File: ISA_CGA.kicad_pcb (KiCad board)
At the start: 4 copper layers, 337.6 x 105.7 mm, 168 parts, among them J1 VIDEO JACK, J2 RGBI Output, P1 1X4 BERG, P2 1X6 BERG, P5 Bus_ISA_8bit, Q1 2N3904, U1 74S112, U10 74153, U101 74S174, U11 74LS74, U12 74LS393, U13 74LS08, U14 74S32, U15 74LS00, U16 74LS04, U17 74LS138, U18 74LS138, U19 74LS138, U2 74LS74, U20 74LS04, U21 74LS174, U22 74LS51, U23 74LS32, U24 74LS244, U25 74LS00, U26 74S04, U27 74LS51, U28 74LS10, U29 74S04, U3 74S86, U30 74LS32, U31 74S08, U32 74LS166, U33 27C256, U34 74LS273, U35 74LS273, U36 74LS244, U37 74LS374, U38 MC6845, U39 74LS174, U4 74S174, U40 74LS174, U41 74LS08, U42 74LS86, U43 74S74, U44 74S74, U45 74LS151, U46 74LS00, U47 74LS51, U48 74LS51, U49 74LS02, U5 74S174, U50 2118, U51 2118, U52 2118, U53 2118, U54 2118, U55 2118, U56 2118, U57 2118, U58 74LS374, U59 74LS374, U6 74LS04, U60 74LS374, U61 74LS374, U62 74LS125, U63 74LS175, U64 74LS164, U65 74LS02, U66 74LS245, U67 74LS244, U68 74LS86, U7 74LS166, U8 74LS166, U9 74153

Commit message: Added copper fill zones
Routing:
- added copper zone on B.Cu, net GND
- added copper zone on F.Cu, net GND
- added copper zone on In1.Cu, net GND
- added copper zone on In2.Cu, net VCC
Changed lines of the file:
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@@
     (connect_pads (clearance 0.508))
     (min_thickness 0.254)
-    (fill yes (arc_segments 32) (thermal_gap 0.508) (thermal_bridge_width 0.508))
+    (fill (arc_segments 32) (thermal_gap 0.508) (thermal_bridge_width 0.508))
     (polygon
       (pts
@@
     (connect_pads (clearance 0.508))
     (min_thickness 0.254)
-    (fill yes (arc_segments 32) (thermal_gap 0.508) (thermal_bridge_width 0.508))
+    (fill (arc_segments 32) (thermal_gap 0.508) (thermal_bridge_width 0.508))
     (polygon
       (pts
@@
       )
     )
+  )
+  (zone (net 2) (net_name GND) (layer B.Cu) (hatch edge 0.508)
+    (connect_pads (clearance 0.508))
+    (min_thickness 0.254)
+    (fill (arc_segments 32) (thermal_gap 0.508) (thermal_bridge_width 0.508))
+    (polygon
+      (pts
+        (xy 376.301 172.212) (xy 260.35 172.212) (xy 260.35 187.706) (xy 30.48 187.706) (xy 30.48 65.659)
+        (xy 376.174 65.659) (xy 376.301 65.532)
+      )
+    )
+  )
+  (zone (net 2) (net_name GND) (layer In1.Cu) (hatch edge 0.508)
+    (connect_pads (clearance 0.508))
+    (min_thickness 0.254)
+    (fill (arc_segments 32) (thermal_gap 0.508) (thermal_bridge_width 0.508))
+    (polygon
+      (pts
+        (xy 376.301 172.198383) (xy 260.35 172.198383) (xy 260.35 187.692383) (xy 30.48 187.692383) (xy 30.48 65.645383)
+        (xy 376.174 65.645383) (xy 376.301 65.518383)
+      )
+    )
+  )
+  (zone (net 2) (net_name GND) (layer F.Cu) (hatch edge 0.508)
+    (connect_pads (clearance 0.508))
+    (min_thickness 0.254)
+    (fill (arc_segments 32) (thermal_gap 0.508) (thermal_bridge_width 0.508))
+    (polygon
+      (pts
+        (xy 376.301 172.198383) (xy 260.35 172.198383) (xy 260.35 187.692383) (xy 30.48 187.692383) (xy 30.48 65.645383)
+        (xy 376.174 65.645383) (xy 376.301 65.518383)
+      )
+    )
+  )
+  (zone (net 1) (net_name VCC) (layer In2.Cu) (hatch edge 0.508)
+    (connect_pads (clearance 0.508))
+    (min_thickness 0.254)
+    (fill (arc_segments 32) (thermal_gap 0.508) (thermal_bridge_width 0.508))
+    (polygon
+      (pts
+        (xy 376.301 172.212) (xy 260.35 172.212) (xy 260.35 187.706) (xy 30.48 187.706) (xy 30.48 65.659)
+        (xy 376.174 65.659) (xy 376.301 65.532)
+      )
+    )

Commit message: Fix connections in power plane
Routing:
- net GND: track 2309.3 -> 2352.5 mm
- net VCC: track 1869.1 -> 1873.5 mm

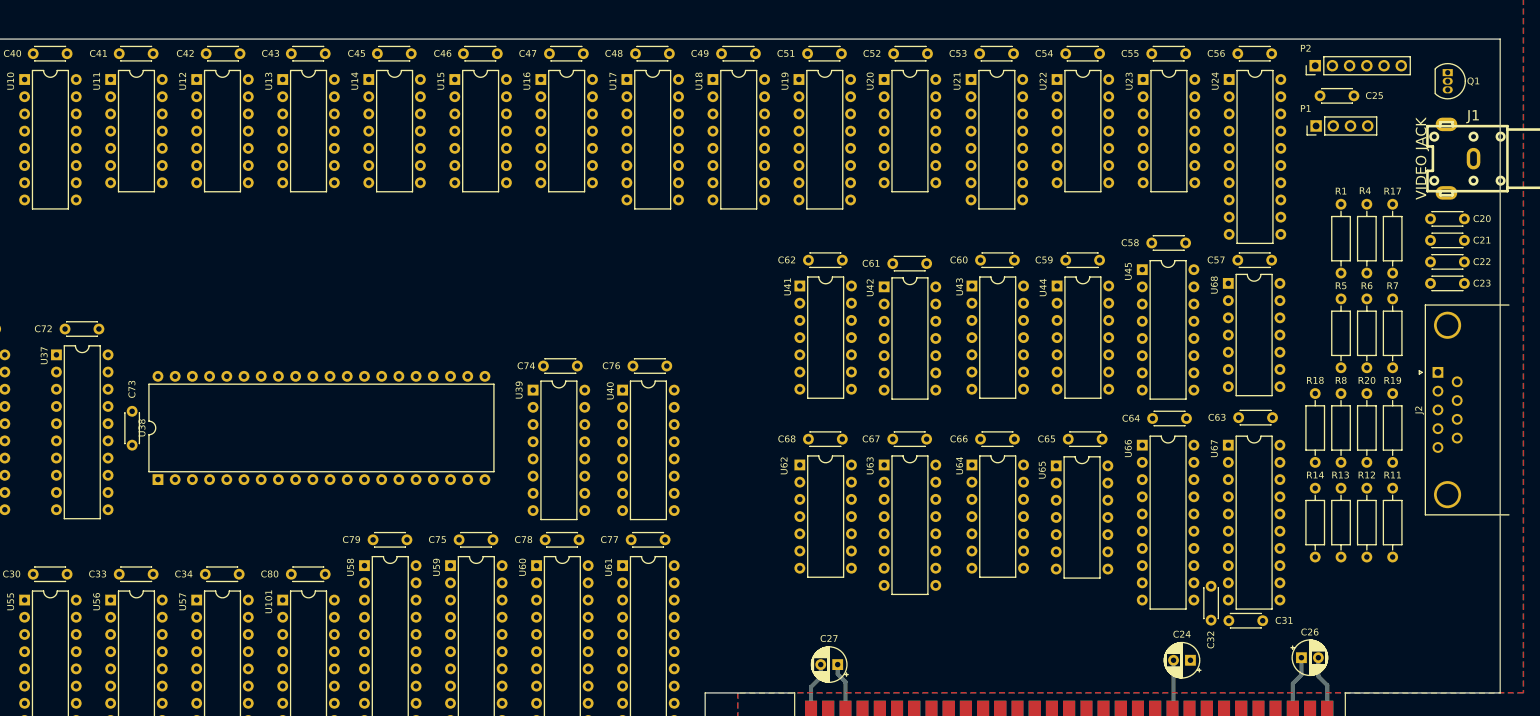
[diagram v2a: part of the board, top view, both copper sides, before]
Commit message: Added some silkscreen
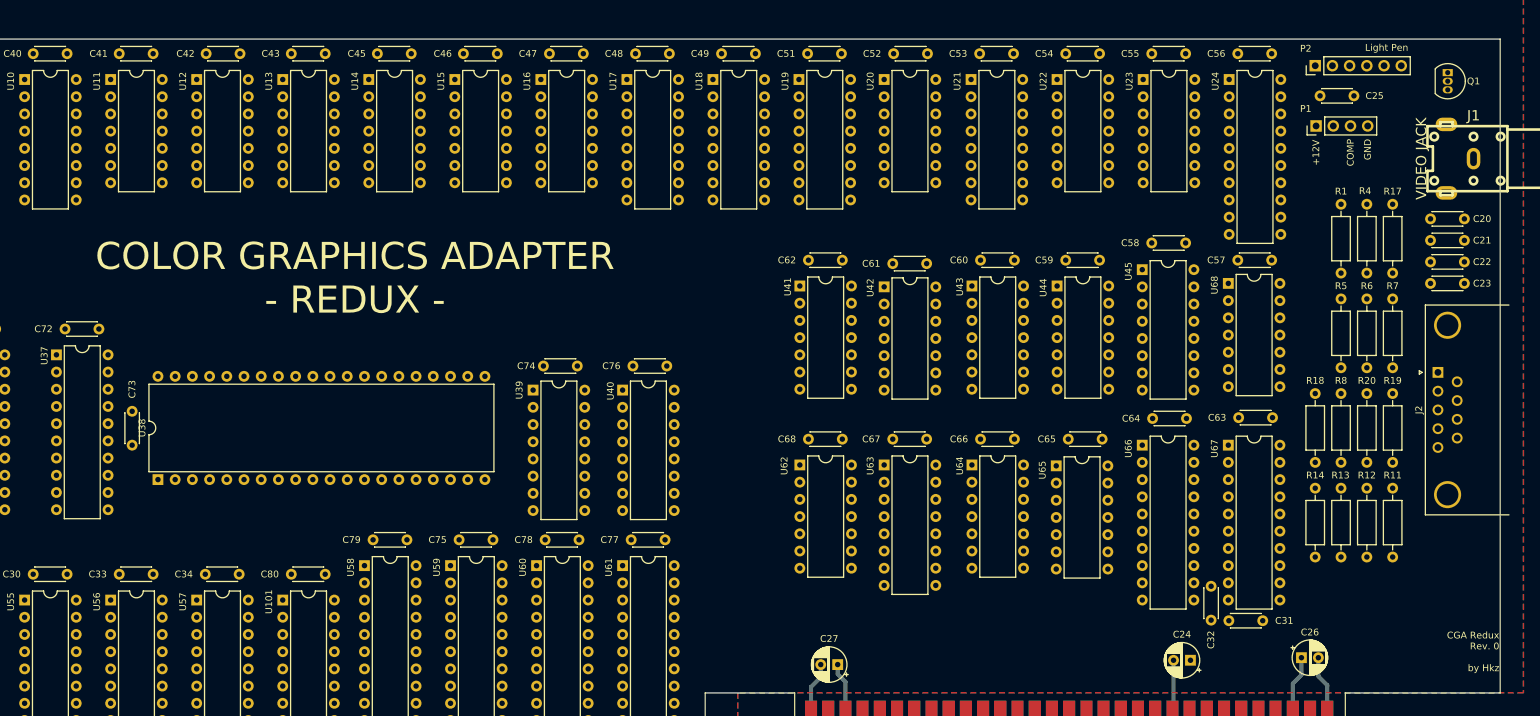
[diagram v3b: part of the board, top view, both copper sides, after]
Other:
- board text added: "+12V"
- board text added: "CGA Redux Rev. 0 by Hkz"
- board text added: "COLOR GRAPHICS ADAPTER - REDUX -"
- board text added: "COMP"
- board text added: "GND"
- board text added: "Light Pen"
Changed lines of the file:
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@@
   (general
     (thickness 1.6)
-    (drawings 21)
+    (drawings 27)
     (tracks 1026)
     (zones 0)
@@
     )
   )
+  (gr_text +12V (at 345.694 90.551 90) (layer F.SilkS)
+    (effects (font (size 1 1) (thickness 0.15)) (justify right))
+  )
+  (gr_text COMP (at 350.774 90.424 90) (layer F.SilkS)
+    (effects (font (size 1 1) (thickness 0.15)) (justify right))
+  )
+  (gr_text GND (at 353.314 90.424 90) (layer F.SilkS)
+    (effects (font (size 1 1) (thickness 0.15)) (justify right))
+  )
+  (gr_text "Light Pen" (at 356.108 76.962) (layer F.SilkS)
+    (effects (font (size 1 1) (thickness 0.15)))
+  )
+  (gr_text "CGA Redux\nRev. 0\n\nby Hkz" (at 372.745 166.116) (layer F.SilkS)
+    (effects (font (size 1 1) (thickness 0.15)) (justify right))
+  )
+  (gr_text "COLOR GRAPHICS ADAPTER\n- REDUX -" (at 203.835 110.998) (layer F.SilkS)
+    (effects (font (size 4 4) (thickness 0.5)))
+  )
   (gr_line (start 90.932 145.288) (end 257.048 145.288) (layer Dwgs.User) (width 0.15))
   (gr_line (start 35.306 75.692) (end 372.872 75.692) (layer Edge.Cuts) (width 0.05))
@@
     )
   )
-  (zone (net 2) (net_name GND) (layer B.Cu) (hatch edge 0.508)
+  (zone (net 2) (net_name GND) (layer In1.Cu) (hatch edge 0.508)
     (connect_pads (clearance 0.508))
     (min_thickness 0.254)
@@
     (polygon
       (pts
-        (xy 376.301 172.212) (xy 260.35 172.212) (xy 260.35 187.706) (xy 30.48 187.706) (xy 30.48 65.659)
-        (xy 376.174 65.659) (xy 376.301 65.532)
+        (xy 376.301 172.198383) (xy 260.35 172.198383) (xy 260.35 187.692383) (xy 30.48 187.692383) (xy 30.48 65.645383)
+        (xy 376.174 65.645383) (xy 376.301 65.518383)
       )
     )
   )
-  (zone (net 2) (net_name GND) (layer In1.Cu) (hatch edge 0.508)
+  (zone (net 2) (net_name GND) (layer F.Cu) (hatch edge 0.508)
     (connect_pads (clearance 0.508))
     (min_thickness 0.254)
@@
     )
   )
-  (zone (net 2) (net_name GND) (layer F.Cu) (hatch edge 0.508)
+  (zone (net 2) (net_name GND) (layer B.Cu) (hatch edge 0.508)
     (connect_pads (clearance 0.508))
     (min_thickness 0.254)
@@
     (polygon
       (pts
-        (xy 376.301 172.198383) (xy 260.35 172.198383) (xy 260.35 187.692383) (xy 30.48 187.692383) (xy 30.48 65.645383)
-        (xy 376.174 65.645383) (xy 376.301 65.518383)
+        (xy 376.301 172.212) (xy 260.35 172.212) (xy 260.35 187.706) (xy 30.48 187.706) (xy 30.48 65.659)
+        (xy 376.174 65.659) (xy 376.301 65.532)
       )
     )

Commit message: Add some more silkscreen entries
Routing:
- net GND: track 2352.5 -> 2343.2 mm
- net VCC: track 1873.5 -> 1865.7 mm

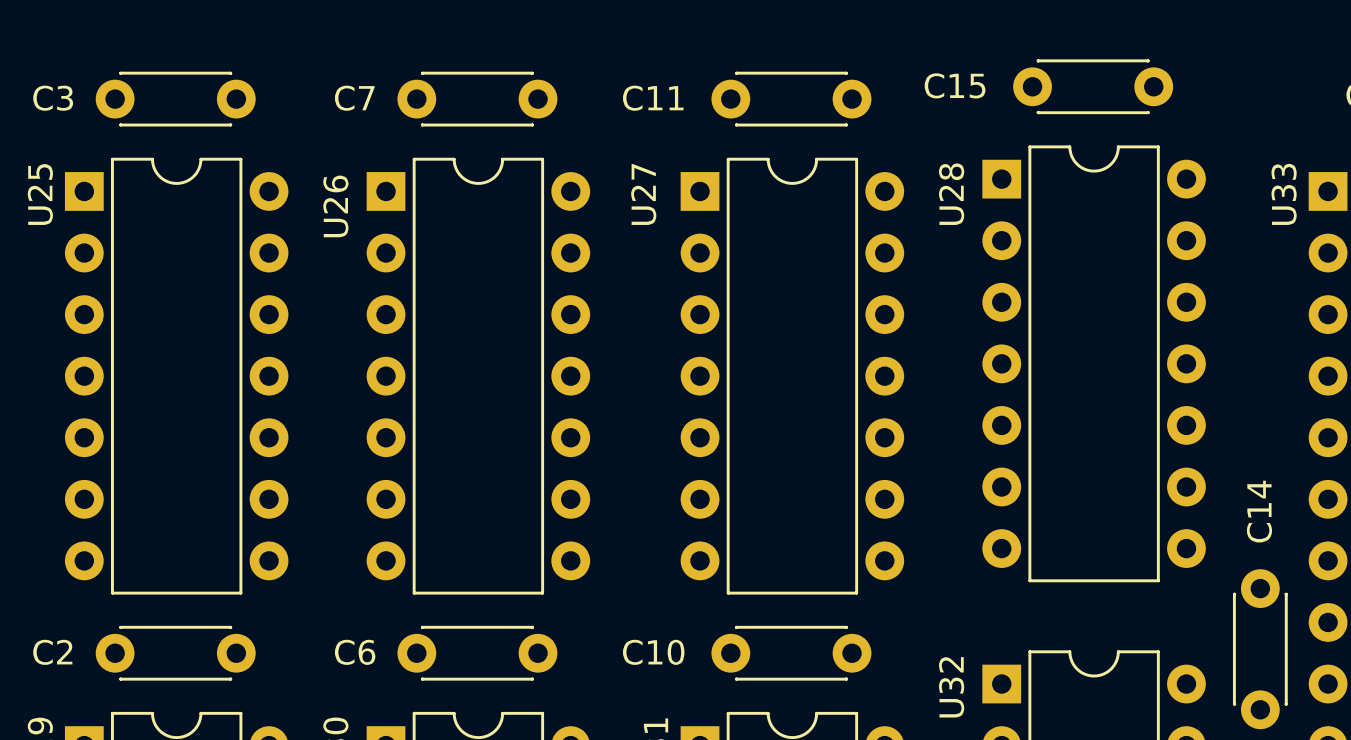
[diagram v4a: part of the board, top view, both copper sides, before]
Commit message: More silkscreen, slightly move component
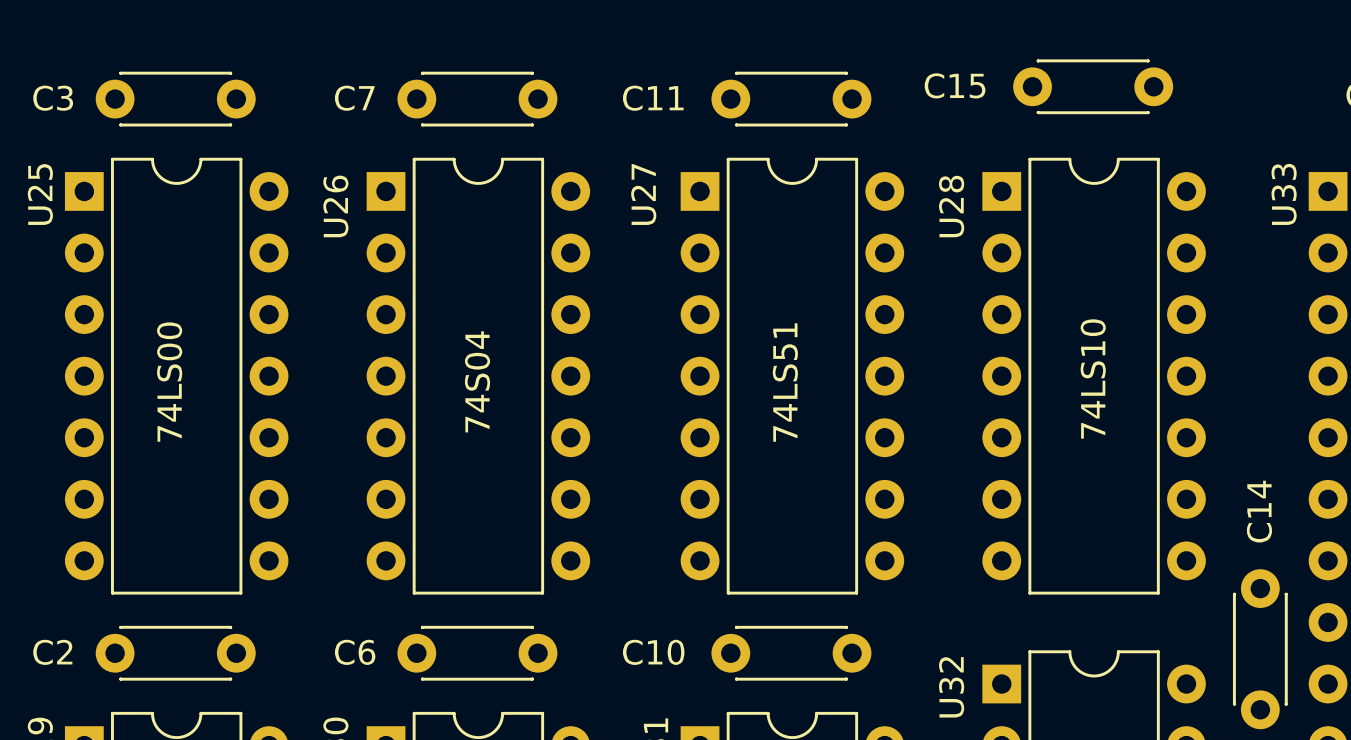
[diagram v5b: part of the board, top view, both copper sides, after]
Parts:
- moved U28 0.51 mm to (78.7, 112.1)
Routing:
- net GND: track 2343.2 -> 2342.6 mm
- net VCC: track 1865.7 -> 1866.2 mm
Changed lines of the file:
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@@
     (thickness 1.6)
     (drawings 27)
-    (tracks 1022)
+    (tracks 1021)
     (zones 0)
     (modules 168)
@@
   )
   (module Package_DIP:DIP-14_W7.62mm (layer F.Cu)
-    (at 78.74 111.633)
+    (at 78.74 112.141)
     (descr "14-lead though-hole mounted DIP package, row spacing 7.62 mm (300 mils)")
     (tags "THT DIP DIL PDIP 2.54mm 7.62mm 300mil")
@@
       (effects (font (size 1 1) (thickness 0.15)))
     )
-    (fp_text value 74LS10 (at 3.81 17.57) (layer F.Fab)
+    (fp_text value 74LS10 (at 3.81 7.747 90) (layer F.SilkS)
       (effects (font (size 1 1) (thickness 0.15)))
     )
@@
       (effects (font (size 1 1) (thickness 0.15)))
     )
-    (fp_text value 74LS51 (at 3.81 17.57) (layer F.Fab)
+    (fp_text value 74LS51 (at 3.556 7.874 90) (layer F.SilkS)
       (effects (font (size 1 1) (thickness 0.15)))
     )
@@
       (effects (font (size 1 1) (thickness 0.15)))
     )
-    (fp_text value 74S04 (at 3.81 17.57) (layer F.Fab)
+    (fp_text value 74S04 (at 3.81 7.874 90) (layer F.SilkS)
       (effects (font (size 1 1) (thickness 0.15)))
     )
@@
       (effects (font (size 1 1) (thickness 0.15)))
     )
-    (fp_text value 74LS00 (at 3.81 17.57) (layer F.Fab)
+    (fp_text value 74LS00 (at 3.556 7.874 90) (layer F.SilkS)
       (effects (font (size 1 1) (thickness 0.15)))
     )
@@
   (segment (start 89.027 107.823) (end 85.01 107.823) (width 0.6) (layer In2.Cu) (net 1))
   (segment (start 92.202 110.998) (end 89.027 107.823) (width 0.6) (layer In2.Cu) (net 1))
-  (segment (start 85.01 110.283) (end 86.36 111.633) (width 0.6) (layer In2.Cu) (net 1))
-  (segment (start 85.01 107.823) (end 85.01 110.283) (width 0.6) (layer In2.Cu) (net 1))
   (segment (start 74.422001 106.472999) (end 72.564 108.331) (width 0.6) (layer In2.Cu) (net 1))
   (segment (start 83.659999 106.472999) (end 74.422001 106.472999) (width 0.6) (layer In2.Cu) (net 1))
@@
   (segment (start 312.085999 106.980999) (end 318.926997 106.980999) (width 0.6) (layer In2.Cu) (net 1))
   (segment (start 312.085999 106.980999) (end 302.514001 106.980999) (width 0.6) (layer In2.Cu) (net 1))
+  (segment (start 85.01 110.791) (end 86.36 112.141) (width 0.6) (layer In2.Cu) (net 1))
+  (segment (start 85.01 107.823) (end 85.01 110.791) (width 0.6) (layer In2.Cu) (net 1))
   (segment (start 53.436999 76.550999) (end 54.737 77.851) (width 0.5) (layer In1.Cu) (net 2))
   (segment (start 43.337001 76.550999) (end 53.436999 76.550999) (width 0.5) (layer In1.Cu) (net 2))
@@
   (segment (start 76.169999 129.890999) (end 78.74 132.461) (width 0.5) (layer In1.Cu) (net 2))
   (segment (start 67.564 131.191) (end 68.864001 129.890999) (width 0.5) (layer In1.Cu) (net 2))
-  (segment (start 78.74 126.873) (end 76.2 129.413) (width 0.5) (layer In1.Cu) (net 2))
-  (segment (start 76.2 129.54) (end 75.849001 129.890999) (width 0.5) (layer In1.Cu) (net 2))
-  (segment (start 76.2 129.413) (end 76.2 129.54) (width 0.5) (layer In1.Cu) (net 2))
   (segment (start 75.849001 129.890999) (end 76.169999 129.890999) (width 0.5) (layer In1.Cu) (net 2))
   (segment (start 68.864001 129.890999) (end 75.849001 129.890999) (width 0.5) (layer In1.Cu) (net 2))
@@
   (segment (start 131.017001 98.090999) (end 131.017001 95.711001) (width 0.6) (layer In1.Cu) (net 2))
   (segment (start 129.667 99.441) (end 131.017001 98.090999) (width 0.6) (layer In1.Cu) (net 2))
+  (segment (start 76.230001 129.890999) (end 76.169999 129.890999) (width 0.6) (layer In1.Cu) (net 2))
+  (segment (start 78.74 127.381) (end 76.230001 129.890999) (width 0.6) (layer In1.Cu) (net 2))
   (zone (net 0) (net_name "") (layers F.Cu In1.Cu In2.Cu B.Cu) (hatch edge 0.508)
     (connect_pads (clearance 0.508))
